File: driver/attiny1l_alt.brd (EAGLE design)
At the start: 26.9 x 17.3 mm, 8 parts, among them IC1 ATTiny85, IC2 LB1973M, IC3 74AHC1G00DCK, J1 AVR_SPI_PRG_6NS

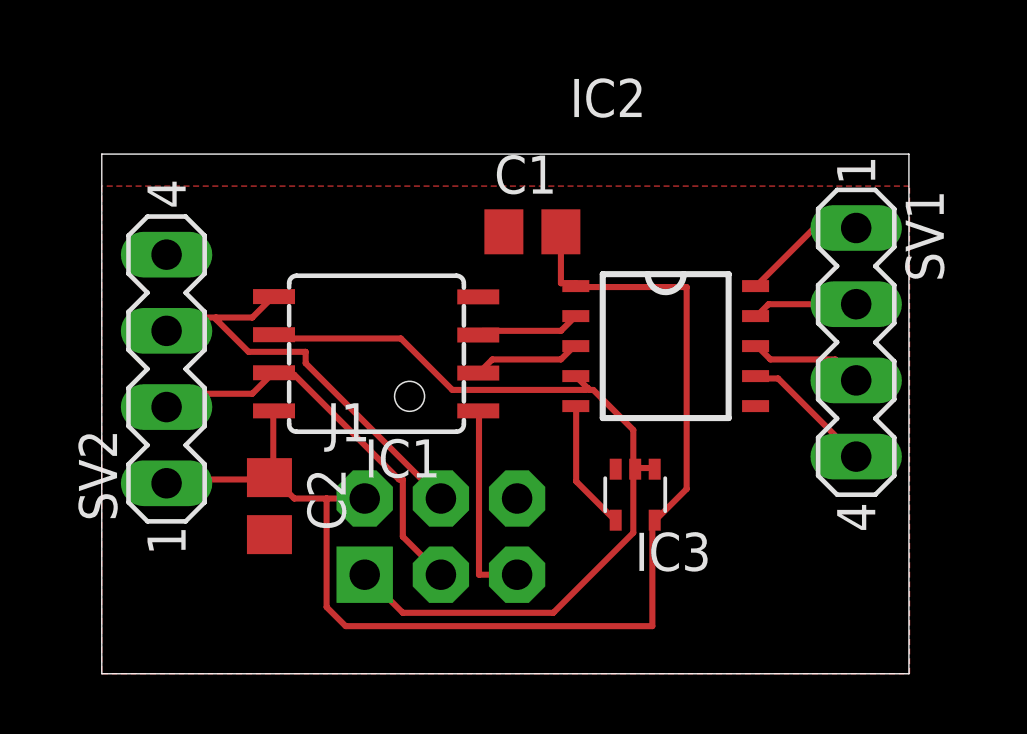
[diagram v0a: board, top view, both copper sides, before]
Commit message: adjust routing for easier home fabrication
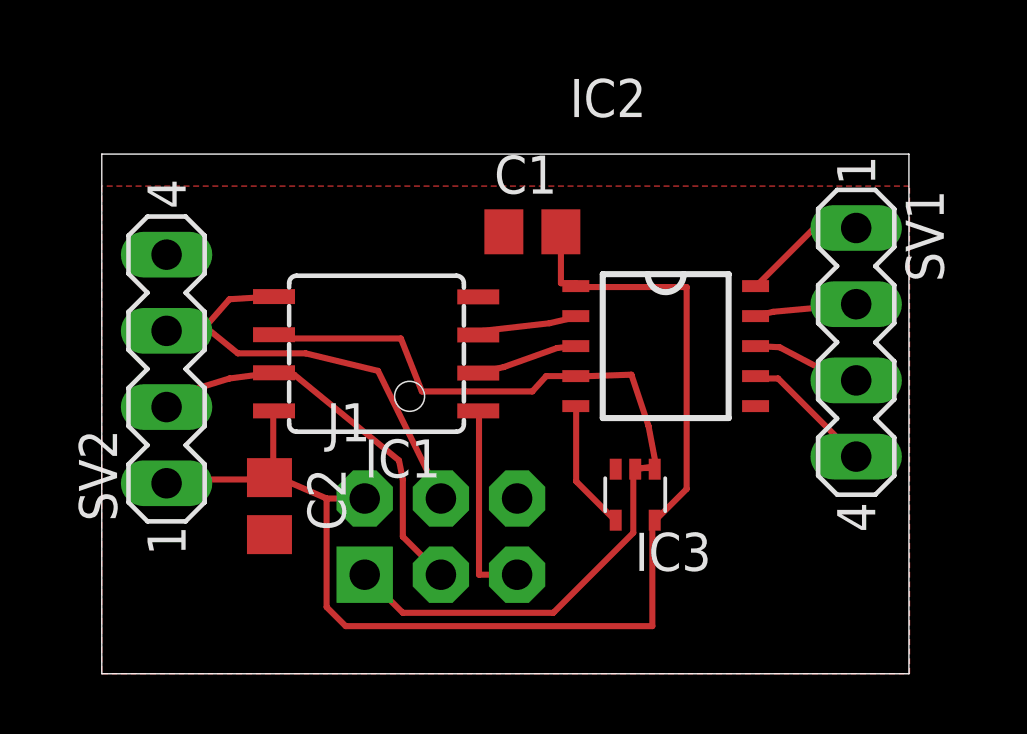
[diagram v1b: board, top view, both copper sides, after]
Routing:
- net IN1/MISO: track 28.7 -> 30.7 mm
- net SDA/MOSI: track 14.3 -> 15.1 mm
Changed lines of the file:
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@@
 <setting verticaltext="up"/>
 </settings>
-<grid distance="5" unitdist="mil" unit="mil" style="lines" multiple="1" display="yes" altdistance="5" altunitdist="mm" altunit="mm"/>
+<grid distance="2" unitdist="mil" unit="mil" style="lines" multiple="1" display="yes" altdistance="5" altunitdist="mm" altunit="mm"/>
 <layers>
 <layer number="1" name="Top" color="4" fill="1" visible="yes" active="yes"/>
@@
 <contactref element="IC1" pad="3"/>
 <contactref element="IC2" pad="2"/>
-<wire x1="15.3035" y1="11.43" x2="15.748" y2="11.8745" width="0.2032" layer="1"/>
-<wire x1="12.7" y1="11.43" x2="15.3035" y2="11.43" width="0.2032" layer="1"/>
+<wire x1="14.9225" y1="11.684" x2="15.748" y2="11.8745" width="0.2032" layer="1"/>
+<wire x1="12.7" y1="11.43" x2="14.9225" y2="11.684" width="0.2032" layer="1"/>
 <wire x1="12.573" y1="11.303" x2="12.7" y2="11.43" width="0.2032" layer="1"/>
 <wire x1="15.748" y1="11.8745" x2="15.8" y2="11.922" width="0.2032" layer="1"/>
@@
 <wire x1="17.78" y1="6.858" x2="17.78" y2="6.819" width="0.2032" layer="1"/>
 <wire x1="18.415" y1="6.858" x2="18.43" y2="6.819" width="0.2032" layer="1"/>
-<wire x1="16.256" y1="9.4615" x2="16.1925" y2="9.525" width="0.2032" layer="1"/>
-<wire x1="16.1925" y1="9.525" x2="15.8115" y2="9.906" width="0.2032" layer="1"/>
-<wire x1="16.383" y1="9.4615" x2="16.256" y2="9.4615" width="0.2032" layer="1"/>
-<wire x1="17.7165" y1="8.128" x2="16.383" y2="9.4615" width="0.2032" layer="1"/>
-<wire x1="17.7165" y1="6.9215" x2="17.7165" y2="8.128" width="0.2032" layer="1"/>
-<wire x1="15.8115" y1="9.906" x2="15.8" y2="9.922" width="0.2032" layer="1"/>
-<wire x1="17.7165" y1="6.9215" x2="17.78" y2="6.819" width="0.2032" layer="1"/>
+<wire x1="17.653" y1="9.9695" x2="15.8115" y2="9.906" width="0.2032" layer="1"/>
+<wire x1="18.2245" y1="8.255" x2="17.653" y2="9.9695" width="0.2032" layer="1"/>
+<wire x1="18.4785" y1="6.9215" x2="18.2245" y2="8.255" width="0.2032" layer="1"/>
+<wire x1="18.4785" y1="6.9215" x2="17.78" y2="6.819" width="0.2032" layer="1"/>
 <wire x1="5.9055" y1="11.176" x2="5.7785" y2="11.303" width="0.2032" layer="1"/>
 <wire x1="9.9695" y1="11.176" x2="5.9055" y2="11.176" width="0.2032" layer="1"/>
-<wire x1="11.684" y1="9.4615" x2="9.9695" y2="11.176" width="0.2032" layer="1"/>
-<wire x1="16.129" y1="9.4615" x2="11.684" y2="9.4615" width="0.2032" layer="1"/>
+<wire x1="10.668" y1="9.4107" x2="9.9695" y2="11.176" width="0.2032" layer="1"/>
+<wire x1="14.351" y1="9.4107" x2="10.668" y2="9.4107" width="0.2032" layer="1"/>
 <wire x1="5.7785" y1="11.303" x2="5.74" y2="11.303" width="0.2032" layer="1"/>
-<wire x1="16.129" y1="9.4615" x2="16.1925" y2="9.525" width="0.2032" layer="1"/>
 <wire x1="10.033" y1="2.032" x2="8.763" y2="3.302" width="0.2032" layer="1"/>
 <wire x1="15.0495" y1="2.032" x2="10.033" y2="2.032" width="0.2032" layer="1"/>
@@
 <wire x1="17.7165" y1="6.731" x2="17.7165" y2="4.699" width="0.2032" layer="1"/>
 <wire x1="17.7165" y1="6.731" x2="17.78" y2="6.819" width="0.2032" layer="1"/>
+<wire x1="15.8" y1="9.922" x2="14.8115" y2="9.922" width="0.2032" layer="1"/>
+<wire x1="14.8115" y1="9.922" x2="14.351" y2="9.4107" width="0.2032" layer="1"/>
+<wire x1="15.8115" y1="9.906" x2="15.8" y2="9.922" width="0" layer="19" extent="1-1"/>
 </signal>
 <signal name="IN3">
 <contactref element="IC1" pad="2"/>
 <contactref element="IC2" pad="3"/>
-<wire x1="15.3035" y1="10.4775" x2="15.748" y2="10.922" width="0.2032" layer="1"/>
-<wire x1="13.0175" y1="10.4775" x2="15.3035" y2="10.4775" width="0.2032" layer="1"/>
-<wire x1="12.573" y1="10.033" x2="13.0175" y2="10.4775" width="0.2032" layer="1"/>
+<wire x1="15.1765" y1="10.8585" x2="15.748" y2="10.922" width="0.2032" layer="1"/>
+<wire x1="13.3985" y1="10.2235" x2="15.1765" y2="10.8585" width="0.2032" layer="1"/>
+<wire x1="12.573" y1="10.033" x2="13.3985" y2="10.2235" width="0.2032" layer="1"/>
 <wire x1="15.748" y1="10.922" x2="15.8" y2="10.922" width="0.2032" layer="1"/>
 <wire x1="12.573" y1="10.033" x2="12.548" y2="10.023" width="0.2032" layer="1"/>
@@
 <contactref element="C1" pad="1"/>
 <contactref element="C2" pad="2"/>
+<wire x1="17.13" y1="6.819" x2="21.792" y2="8.922" width="0" layer="19" extent="1-1"/>
 <wire x1="13.843" y1="5.842" x2="17.13" y2="6.819" width="0" layer="19" extent="1-1"/>
-<wire x1="21.792" y1="8.922" x2="17.13" y2="6.819" width="0" layer="19" extent="1-1"/>
 </signal>
 <signal name="+5V">
@@
 <wire x1="5.715" y1="8.763" x2="5.74" y2="8.763" width="0.2032" layer="1"/>
 <wire x1="5.588" y1="6.5405" x2="5.588" y2="6.538" width="0.2032" layer="1"/>
-<wire x1="6.4135" y1="5.842" x2="5.7785" y2="6.477" width="0.2032" layer="1"/>
+<wire x1="6.0325" y1="6.477" x2="5.7785" y2="6.477" width="0.2032" layer="1"/>
 <wire x1="8.763" y1="5.842" x2="7.493" y2="5.842" width="0.2032" layer="1"/>
-<wire x1="7.493" y1="5.842" x2="6.4135" y2="5.842" width="0.2032" layer="1"/>
+<wire x1="7.493" y1="5.842" x2="6.0325" y2="6.477" width="0.2032" layer="1"/>
 <wire x1="5.7785" y1="6.477" x2="5.588" y2="6.538" width="0.2032" layer="1"/>
 <wire x1="2.286" y1="6.477" x2="2.159" y2="6.35" width="0.2032" layer="1"/>
@@
 <contactref element="J1" pad="4"/>
 <contactref element="SV2" pad="3"/>
-<wire x1="5.0165" y1="11.8745" x2="5.715" y2="12.573" width="0.2032" layer="1"/>
-<wire x1="2.6035" y1="11.8745" x2="3.81" y2="11.8745" width="0.2032" layer="1"/>
-<wire x1="3.81" y1="11.8745" x2="5.0165" y2="11.8745" width="0.2032" layer="1"/>
+<wire x1="4.2545" y1="12.4841" x2="5.715" y2="12.573" width="0.2032" layer="1"/>
+<wire x1="2.6035" y1="11.8745" x2="3.4544" y2="11.5697" width="0.2032" layer="1"/>
+<wire x1="3.4544" y1="11.5697" x2="4.2545" y2="12.4841" width="0.2032" layer="1"/>
 <wire x1="2.159" y1="11.43" x2="2.6035" y2="11.8745" width="0.2032" layer="1"/>
 <wire x1="5.715" y1="12.573" x2="5.74" y2="12.573" width="0.2032" layer="1"/>
-<wire x1="6.7945" y1="10.3505" x2="11.303" y2="5.842" width="0.2032" layer="1"/>
-<wire x1="6.7945" y1="10.7315" x2="6.7945" y2="10.3505" width="0.2032" layer="1"/>
-<wire x1="4.8895" y1="10.7315" x2="6.7945" y2="10.7315" width="0.2032" layer="1"/>
-<wire x1="3.81" y1="11.811" x2="4.8895" y2="10.7315" width="0.2032" layer="1"/>
-<wire x1="3.81" y1="11.811" x2="3.81" y2="11.8745" width="0.2032" layer="1"/>
+<wire x1="9.2075" y1="10.0965" x2="11.303" y2="5.842" width="0.2032" layer="1"/>
+<wire x1="6.7945" y1="10.6807" x2="9.2075" y2="10.0965" width="0.2032" layer="1"/>
+<wire x1="4.5339" y1="10.6807" x2="6.7945" y2="10.6807" width="0.2032" layer="1"/>
+<wire x1="3.4544" y1="11.557" x2="4.5339" y2="10.6807" width="0.2032" layer="1"/>
+<wire x1="3.4544" y1="11.557" x2="3.4544" y2="11.5697" width="0.2032" layer="1"/>
 </signal>
 <signal name="RESET-">
@@
 <contactref element="J1" pad="3"/>
 <contactref element="SV2" pad="2"/>
-<wire x1="5.0165" y1="9.3345" x2="5.715" y2="10.033" width="0.2032" layer="1"/>
-<wire x1="2.6035" y1="9.3345" x2="5.0165" y2="9.3345" width="0.2032" layer="1"/>
+<wire x1="4.2545" y1="9.8425" x2="5.715" y2="10.033" width="0.2032" layer="1"/>
+<wire x1="2.6035" y1="9.3345" x2="4.2545" y2="9.8425" width="0.2032" layer="1"/>
 <wire x1="2.159" y1="8.89" x2="2.6035" y2="9.3345" width="0.2032" layer="1"/>
 <wire x1="5.715" y1="10.033" x2="5.74" y2="10.033" width="0.2032" layer="1"/>
 <wire x1="10.033" y1="4.572" x2="11.303" y2="3.302" width="0.2032" layer="1"/>
 <wire x1="10.033" y1="6.477" x2="10.033" y2="4.572" width="0.2032" layer="1"/>
-<wire x1="9.906" y1="6.477" x2="10.033" y2="6.477" width="0.2032" layer="1"/>
-<wire x1="6.4135" y1="9.9695" x2="9.906" y2="6.477" width="0.2032" layer="1"/>
+<wire x1="9.906" y1="7.112" x2="10.033" y2="6.477" width="0.2032" layer="1"/>
+<wire x1="6.4135" y1="9.9695" x2="9.906" y2="7.112" width="0.2032" layer="1"/>
 <wire x1="5.7785" y1="9.9695" x2="6.4135" y2="9.9695" width="0.2032" layer="1"/>
 <wire x1="5.7785" y1="9.9695" x2="5.74" y2="10.033" width="0.2032" layer="1"/>
@@
 <contactref element="SV1" pad="2"/>
 <contactref element="IC2" pad="9"/>
-<wire x1="22.225" y1="12.319" x2="21.844" y2="11.938" width="0.2032" layer="1"/>
-<wire x1="25.146" y1="12.319" x2="22.225" y2="12.319" width="0.2032" layer="1"/>
+<wire x1="22.3774" y1="12.065" x2="21.844" y2="11.938" width="0.2032" layer="1"/>
+<wire x1="25.146" y1="12.319" x2="22.3774" y2="12.065" width="0.2032" layer="1"/>
 <wire x1="21.844" y1="11.938" x2="21.792" y2="11.922" width="0.2032" layer="1"/>
 </signal>
@@
 <contactref element="SV1" pad="3"/>
 <contactref element="IC2" pad="8"/>
-<wire x1="22.2885" y1="10.4775" x2="21.844" y2="10.922" width="0.2032" layer="1"/>
-<wire x1="24.4475" y1="10.4775" x2="22.2885" y2="10.4775" width="0.2032" layer="1"/>
-<wire x1="25.146" y1="9.779" x2="24.4475" y2="10.4775" width="0.2032" layer="1"/>
+<wire x1="22.5933" y1="10.8839" x2="21.844" y2="10.922" width="0.2032" layer="1"/>
+<wire x1="24.1427" y1="10.0711" x2="22.5933" y2="10.8839" width="0.2032" layer="1"/>
+<wire x1="25.146" y1="9.779" x2="24.1427" y2="10.0711" width="0.2032" layer="1"/>
 <wire x1="21.844" y1="10.922" x2="21.792" y2="10.922" width="0.2032" layer="1"/>
 </signal>

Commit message: added some more jumper to hopefully get better ground connections
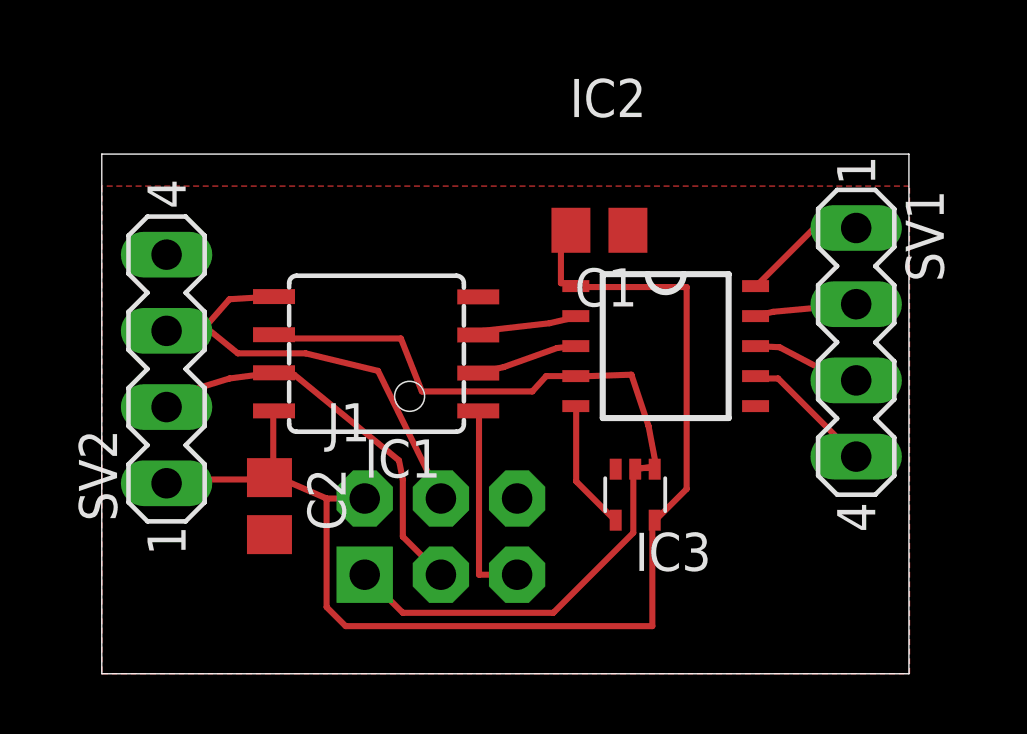
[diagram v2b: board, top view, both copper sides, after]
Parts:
- moved C1 2.24 mm to (16.6, 14.8), turned to 180 degrees
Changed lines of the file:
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@@
 </element>
 <element name="IC2" library="LB1973M" package="SSOP10" value="LB1973M" x="18.796" y="10.922"/>
-<element name="C1" library="rcl" package="C0805" value="" x="14.351" y="14.732"/>
+<element name="C1" library="rcl" package="C0805" value="" x="16.5862" y="14.7828" rot="R180"/>
 <element name="C2" library="rcl" package="C0805" value="" x="5.588" y="5.588" rot="R270"/>
 </elements>
@@
 <contactref element="C1" pad="1"/>
 <contactref element="C2" pad="2"/>
-<wire x1="17.13" y1="6.819" x2="21.792" y2="8.922" width="0" layer="19" extent="1-1"/>
-<wire x1="13.843" y1="5.842" x2="17.13" y2="6.819" width="0" layer="19" extent="1-1"/>
+<wire x1="17.13" y1="6.819" x2="13.843" y2="5.842" width="0" layer="19" extent="1-1"/>
+<wire x1="21.792" y1="8.922" x2="17.13" y2="6.819" width="0" layer="19" extent="1-1"/>
 </signal>
 <signal name="+5V">
@@
 <wire x1="15.3035" y1="13.0175" x2="15.3035" y2="14.732" width="0.2032" layer="1"/>
 <wire x1="15.8115" y1="13.0175" x2="15.3035" y2="13.0175" width="0.2032" layer="1"/>
-<wire x1="15.3035" y1="14.732" x2="15.301" y2="14.732" width="0.2032" layer="1"/>
+<wire x1="15.3035" y1="14.732" x2="15.6362" y2="14.7828" width="0.2032" layer="1"/>
 <wire x1="15.8115" y1="13.0175" x2="15.8" y2="12.922" width="0.2032" layer="1"/>
 <wire x1="5.715" y1="6.5405" x2="5.715" y2="8.763" width="0.2032" layer="1"/>
